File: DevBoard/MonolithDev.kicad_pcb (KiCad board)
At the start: 6 copper layers, 196 x 115 mm, 417 parts, among them J101 Pack (welded 4S) - use instea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, J102 Cell 1 NTC 10k 103AT, J103 EV2400 SMBus, J104 Bench PACK_P, J105 Cell 2 NTC 10k 103AT, J106 Cell 3 NTC 10k 103AT, J107 Cell 4 NTC 10k 103AT, J301 SWD, J302 UART debug, J303 Spare GPIO, J401 TYPE-C 16PCB1.6 IP68, J402 I2CC logic analyzer, J501 TYPE-C 16PCB1.6 IP68, J502 I2CC logic analyzer, Q101 AGM404AP1, Q102 AGM404AP1, Q103 AO3400A, Q104 AO3400A, Q401 PGQ04N070, Q402 PGQ04N070, Q403 AO3401A, Q404 AO3401A, Q405 AO3400A, Q406 AO3400A, Q407 PGQ04N070, Q408 PGQ04N070, Q501 PGQ04N070, Q502 PGQ04N070, Q503 AO3401A, Q504 AO3401A, Q505 AO3400A, Q506 AO3400A, Q507 PGQ04N070, Q508 PGQ04N070, SW101 WAKE, SW301 RESET, U101 BQ40Z50RSMR-R2, U102 BQ294700DSGR, U201 INA190A5IDDFR, U202 INA190A1IDDFR, U203 HT7550-1, U204 TPS62177DQCR, U301 CC2340R5MODA, U302 TMP1075, U303 TMP1075, U304 TMP1075, U305 TMP1075, U306 TMP1075, U401 TPS25751DREFR, U402 M24512-DFMC6TG, U403 BQ25756RRVR, U404 TPS62933DRLR, U405 TPD4S201TRGRRQ1, U501 TPS25751DREFR, U502 M24512-DFMC6TG, U503 BQ25756RRVR, U504 TPS62933DRLR, U505 TPD4S201TRGRRQ1

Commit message: Dev board rev A8: review 4 pre-routing hardware fixes
Applied by tools/review4_fixes.py (one-shot from the rev A7 sheets);
part numbers checked against JLC's parts API.
- R313 470k -> 220k (3V3_SLEEP margin), R314 100k -> 47k (IRQ_N),
  R304/R305 4.7k -> 3.3k (I2C rise time)
- R322/R323 1k in series with J302 TX/RX; R324 1k at J303 pin 2
- C314 placeholder 1p C0G (DNP); C401/C402 330p -> 220p (CC capacitance)
- R450/R451 snubber resistors -> 1206 0.66 W (a 2010/0612 doesn't fit)
- D401/D501 SMAJ22A -> TVS2200DRVR flat clamp (stock KiCad symbol and
  footprint; datasheet added)
- TP415-TP421 (+5xx) 1 mm probe pads on CC, SBU and liquid-detect nets
Board synced and placed (place_blocks.py): 428 parts, 0 parity issues,
no courtyard overlaps. ERC: the 8 known warnings. README item 41,
schematic PDF and placement PNG regenerated.

Co-Authored-By: Claude Opus 5.5 <noreply@anthropic.com>
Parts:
- added R322: 1k, Resistor_SMD:R_0603_1608Metric, F.Cu at (182.8, 60.6)
- added R323: 1k, Resistor_SMD:R_0603_1608Metric, F.Cu at (184.6, 60.6)
- added R324: 1k, Resistor_SMD:R_0603_1608Metric, F.Cu at (220.5, 60.6)
- added TP415: CC1, TestPoint:TestPoint_Pad_D1.0mm, F.Cu at (231.0, 77.1)
- added TP416: CC2, TestPoint:TestPoint_Pad_D1.0mm, F.Cu at (228.4, 77.1)
- added TP417: SBU_FLT, TestPoint:TestPoint_Pad_D1.0mm, F.Cu at (237.5, 76.6)
- added TP418: SBU1_SNS, TestPoint:TestPoint_Pad_D1.0mm, F.Cu at (237.5, 79.2)
- added TP419: SBU2_SNS, TestPoint:TestPoint_Pad_D1.0mm, F.Cu at (237.5, 81.8)
- added TP420: LIQ_PU, TestPoint:TestPoint_Pad_D1.0mm, F.Cu at (224.7, 64.0)
- added TP421: LIQ_PD, TestPoint:TestPoint_Pad_D1.0mm, F.Cu at (220.3, 73.4)
- added TP515: CC1, TestPoint:TestPoint_Pad_D1.0mm, F.Cu at (231.0, 113.1)
- added TP516: CC2, TestPoint:TestPoint_Pad_D1.0mm, F.Cu at (228.4, 113.1)
- added TP517: SBU_FLT, TestPoint:TestPoint_Pad_D1.0mm, F.Cu at (237.5, 112.6)
- added TP518: SBU1_SNS, TestPoint:TestPoint_Pad_D1.0mm, F.Cu at (237.5, 115.2)
- added TP519: SBU2_SNS, TestPoint:TestPoint_Pad_D1.0mm, F.Cu at (237.5, 117.8)
- added TP520: LIQ_PU, TestPoint:TestPoint_Pad_D1.0mm, F.Cu at (224.7, 100.0)
- added TP521: LIQ_PD, TestPoint:TestPoint_Pad_D1.0mm, F.Cu at (220.3, 109.4)
- C314: value TBD -> 1p C0G
- C401, C402, C501, C502: value 330p 50V -> 220p 50V
- D401, D501: value SMAJ22A -> TVS2200DRVR; footprint Diode_SMD:D_SMA -> Package_SON:WSON-6-1EP_2x2mm_P0.65mm_EP1x1.6mm
- R304, R305: value 4.7k -> 3.3k
- R313: value 470k -> 220k
- R314: value 100k -> 47k
- R450, R451, R550, R551: footprint Resistor_SMD:R_0805_2012Metric -> Resistor_SMD:R_1206_3216Metric
- moved R451 0.41 mm to (198.1, 88.0)
- moved R551 0.41 mm to (198.1, 124.0)
- moved R450 0.40 mm to (217.1, 88.0)
- moved R550 0.40 mm to (217.1, 124.0)
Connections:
- D401 pad 1: /USB Port 1/VBUS -> GND
- D501 pad 1: /USB Port 2/VBUS -> GND
- J302 pad 1: /MCU and NTCs/UART_TX -> Net-(J302-Pin_1)
- J302 pad 2: /MCU and NTCs/UART_RX -> Net-(J302-Pin_2)
- J303 pad 2: IRQ_N -> Net-(J303-Pin_2)

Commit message: Dev board rev A8 part 2: review 4 docs, BOM, A-2 procedure, J104 clamp
Schematic edits by tools/review4_docs.py (helpers split out of
review4_fixes.py into tools/sch_edit.py; review4_fixes output unchanged).
- A-2: EV2400 work only with 3V3 up (J104) and U301 in reset; checklist,
  R312/R301 Notes and MCU sheet note 10 rewritten.
- D-5: D105 SMAJ18A clamp on the J104 side of D104; board placed
  (D104 moved one body width left).
- Stale Notes, sheet notes, heading and address text fixed; sheet 4
  renamed "MCU and Sensors"; revision log A7/A8; title blocks A8.
- MPNs filled on the parts that had only LCSC numbers; Sourcing on U301
  and J301; J301 out of the position file.
- bringup-config-checklist, mcu-io-power-states and power-budget rewritten
  for the CC2340 with every review 4 CONFIG item; corrections in
  circuit-description, cost-down and cc2340-pin-budget.
ERC: 8 known warnings. 0 text overlaps. DRC: 0 parity issues, no
courtyard overlaps (429 parts). README item 42.

Co-Authored-By: Claude Opus 5.5 <noreply@anthropic.com>
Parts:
- added D105: SMAJ18A, Diode_SMD:D_SMA, F.Cu at (171.9, 106.4)
- R127: value 0R DNP -> 0R
- TP107: value GAUGE_BTP -> IRQ_N
- moved D104 7.85 mm to (164.1, 106.4)
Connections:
- net /MCU and NTCs/3V3_MCU renamed /MCU and Sensors/3V3_MCU
- net /MCU and NTCs/ANT_IN renamed /MCU and Sensors/ANT_IN
- net /MCU and NTCs/J303_CHG_INH renamed /MCU and Sensors/J303_CHG_INH
- net /MCU and NTCs/J303_EN_5V1 renamed /MCU and Sensors/J303_EN_5V1
- net /MCU and NTCs/J303_EN_5V2 renamed /MCU and Sensors/J303_EN_5V2
- net /MCU and NTCs/LED_DRV renamed /MCU and Sensors/LED_DRV
- net /MCU and NTCs/NRST renamed /MCU and Sensors/NRST
- net /MCU and NTCs/RFIO renamed /MCU and Sensors/RFIO
- net /MCU and NTCs/SMB_PU renamed /MCU and Sensors/SMB_PU
- net /MCU and NTCs/UART_RX renamed /MCU and Sensors/UART_RX
- net /MCU and NTCs/UART_TX renamed /MCU and Sensors/UART_TX

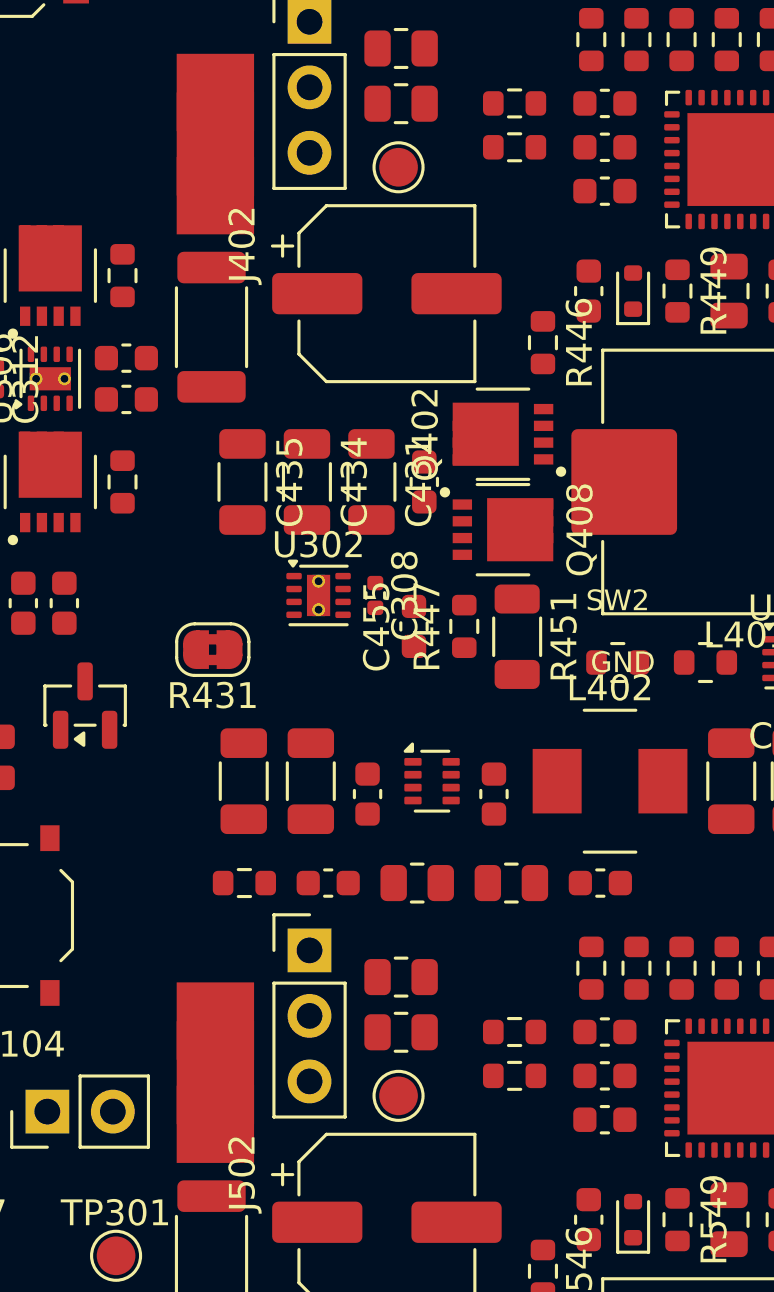
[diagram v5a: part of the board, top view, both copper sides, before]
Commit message: Dev board: hybrid battery-side bulk, ship mode at 5 % SOC, CC2340 in stock
- C432/C532 (battery-side bulk, the only bulk cap biased in idle) ->
  Panasonic EEH-ZA1E101XP hybrid polymer (C264047), CP_Elec_6.3x7.7.
  Same 100 uF / 30 mOhm as the JIERR solid polymer, but leakage limit
  0.01CV = 25 uA instead of 0.2CV = 500 uA. +$1.28 per board. README
  item 43; review 4 B-4 closed. Board synced: 0 parity issues, no
  courtyard overlaps.
- Ship mode also triggers at RSOC <= 5 % (checklist, power states,
  review 4 S-1).
- CC2340R5MODA is in stock at TI.com (seen logged in, 2026-10-15):
  U301 Sourcing, bom_cost.py, checklist and README notes updated.

Co-Authored-By: Claude Opus 5.5 <noreply@anthropic.com>
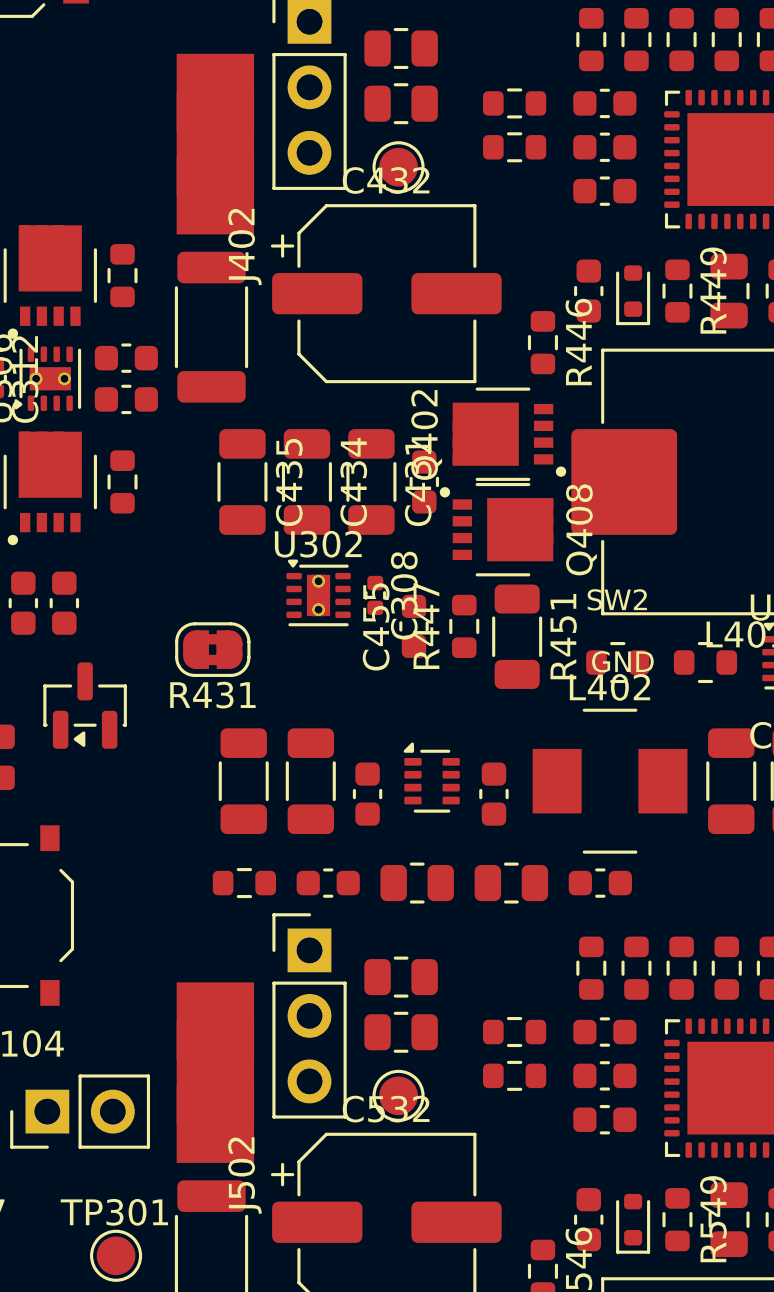
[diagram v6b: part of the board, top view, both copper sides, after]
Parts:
- C432, C532: footprint Capacitor_SMD:CP_Elec_6.3x5.8 -> Capacitor_SMD:CP_Elec_6.3x7.7

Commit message: Dev board: cut JLC extended parts 37 -> 27 for a 2-board build
tools/bom_fee_cut.py (one-shot); README item 44. At 2 boards the costed
BOM goes from $124.28 to $108.49 per board.
- Basic/preferred swaps, no footprint changes: C313 -> C1548, C315/C314
  -> C1550, C401/C402 -> C1530 (X7R), R433/R434 -> 120k/22k 1 %
  (PP5V 5.16 V), C443/C543 -> 100 uF 35 V Honor polymer (same as C421).
- Hand-fit from LCSC: BT101-BT104, the 13 Harwin test loops, U202, D105
  (dev-only; out of the position file).
- Board: fields refreshed by netlist_to_board.py; also includes Logan's
  block move made in KiCad. DRC parity 0; ERC unchanged.

Co-Authored-By: Claude Opus 5.5 <noreply@anthropic.com>
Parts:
- C443, C543: value 220u 16V -> 100u 35V
- R433, R533: value 107k 0.1% -> 120k
- R434, R534: value 20.0k 0.1% -> 22k
- moved D104 227.1 mm to (377.0, 27.5)
- moved D105 224.8 mm to (383.8, 31.2)
- moved J104 217.4 mm to (382.5, 27.5)
- moved SW101 208.4 mm to (366.4, 9.50)
- moved R114 201.7 mm to (361.3, 21.4), turned to 180 degrees
- moved R117 201.1 mm to (357.3, 18.9), turned to 0 degrees
- moved R115 191.6 mm to (345.6, 0.00)
- moved R116 191.6 mm to (345.6, 1.59)
- moved C107 191.0 mm to (348.0, -5.20)
- moved C109 191.0 mm to (338.4, -9.90)
- moved R101 191.0 mm to (330.1, 3.20)
- moved R102 191.0 mm to (330.1, 0.70)
- moved R103 191.0 mm to (330.1, -1.80)
- moved R104 191.0 mm to (330.1, -4.30)
- moved R106 191.0 mm to (343.8, -4.70)
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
